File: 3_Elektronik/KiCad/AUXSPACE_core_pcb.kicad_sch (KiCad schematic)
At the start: 4 parts

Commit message: BOM:              added missing datasheets, added missing partnumbers, corrected partnumbers circit diagram:   adjusted values unified writing
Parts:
- R1, R3, R5, R7: WE_PTNBR (none) -> 560112116001
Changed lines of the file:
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@@
 			)
 		)
-		(property "Datasheet" ""
+		(property "Datasheet" "https://www.we-online.com/components/products/datasheet/560112116001.pdf"
 			(at 245.11 125.73 0)
 			(hide yes)
@@
 		(property "Description" "Resistor"
 			(at 245.11 125.73 0)
+			(hide yes)
+			(show_name no)
+			(do_not_autoplace no)
+			(effects
+				(font
+					(size 1.27 1.27)
+				)
+			)
+		)
+		(property "LCSC_PTNBR" ""
+			(at 245.11 125.73 90)
+			(hide yes)
+			(show_name no)
+			(do_not_autoplace no)
+			(effects
+				(font
+					(size 1.27 1.27)
+				)
+			)
+		)
+		(property "WE_PTNBR" "560112116001"
+			(at 245.11 125.73 90)
+			(hide yes)
+			(show_name no)
+			(do_not_autoplace no)
+			(effects
+				(font
+					(size 1.27 1.27)
+				)
+			)
+		)
+		(property "VOELKNER_PTNBR" ""
+			(at 245.11 125.73 90)
+			(hide yes)
+			(show_name no)
+			(do_not_autoplace no)
+			(effects
+				(font
+					(size 1.27 1.27)
+				)
+			)
+		)
+		(property "MOUSER_PTNBR" ""
+			(at 245.11 125.73 90)
 			(hide yes)
 			(show_name no)
@@
 			)
 		)
-		(property "Datasheet" ""
+		(property "Datasheet" "https://www.we-online.com/components/products/datasheet/560112116001.pdf"
 			(at 245.11 132.08 0)
 			(hide yes)
@@
 		(property "Description" "Resistor"
 			(at 245.11 132.08 0)
+			(hide yes)
+			(show_name no)
+			(do_not_autoplace no)
+			(effects
+				(font
+					(size 1.27 1.27)
+				)
+			)
+		)
+		(property "LCSC_PTNBR" ""
+			(at 245.11 132.08 90)
+			(hide yes)
+			(show_name no)
+			(do_not_autoplace no)
+			(effects
+				(font
+					(size 1.27 1.27)
+				)
+			)
+		)
+		(property "WE_PTNBR" "560112116001"
+			(at 245.11 132.08 90)
+			(hide yes)
+			(show_name no)
+			(do_not_autoplace no)
+			(effects
+				(font
+					(size 1.27 1.27)
+				)
+			)
+		)
+		(property "VOELKNER_PTNBR" ""
+			(at 245.11 132.08 90)
+			(hide yes)
+			(show_name no)
+			(do_not_autoplace no)
+			(effects
+				(font
+					(size 1.27 1.27)
+				)
+			)
+		)
+		(property "MOUSER_PTNBR" ""
+			(at 245.11 132.08 90)
 			(hide yes)
 			(show_name no)
@@
 			)
 		)
-		(property "Datasheet" ""
+		(property "Datasheet" "https://www.we-online.com/components/products/datasheet/560112116001.pdf"
 			(at 245.11 119.38 0)
 			(hide yes)
@@
 		(property "Description" "Resistor"
 			(at 245.11 119.38 0)
+			(hide yes)
+			(show_name no)
+			(do_not_autoplace no)
+			(effects
+				(font
+					(size 1.27 1.27)
+				)
+			)
+		)
+		(property "LCSC_PTNBR" ""
+			(at 245.11 119.38 90)
+			(hide yes)
+			(show_name no)
+			(do_not_autoplace no)
+			(effects
+				(font
+					(size 1.27 1.27)
+				)
+			)
+		)
+		(property "WE_PTNBR" "560112116001"
+			(at 245.11 119.38 90)
+			(hide yes)
+			(show_name no)
+			(do_not_autoplace no)
+			(effects
+				(font
+					(size 1.27 1.27)
+				)
+			)
+		)
+		(property "VOELKNER_PTNBR" ""
+			(at 245.11 119.38 90)
+			(hide yes)
+			(show_name no)
+			(do_not_autoplace no)
+			(effects
+				(font
+					(size 1.27 1.27)
+				)
+			)
+		)
+		(property "MOUSER_PTNBR" ""
+			(at 245.11 119.38 90)
 			(hide yes)
 			(show_name no)
@@
 			)
 		)
-		(property "Datasheet" ""
+		(property "Datasheet" "https://www.we-online.com/components/products/datasheet/560112116001.pdf"
 			(at 245.11 113.03 0)
 			(hide yes)
@@
 			(hide yes)
 			(show_name no)
+			(do_not_autoplace no)
+			(effects
+				(font
+					(size 1.27 1.27)
+				)
+			)
+		)
+		(property "LCSC_PTNBR" ""
+			(at 245.11 113.03 90)
+			(hide yes)
+			(show_name no)
+			(do_not_autoplace no)
+			(effects
+				(font
+					(size 1.27 1.27)
+				)
+			)
+		)
+		(property "WE_PTNBR" "560112116001"
+			(at 245.11 113.03 90)
+			(hide yes)
+			(show_name no)
+			(do_not_autoplace no)
+			(effects
+				(font
+					(size 1.27 1.27)
+				)
+			)
+		)
+		(property "VOELKNER_PTNBR" ""
+			(at 245.11 113.03 90)
+			(hide yes)
+			(show_name no)
+			(do_not_autoplace no)
+			(effects
+				(font
+					(size 1.27 1.27)
+				)
+			)
+		)
+		(property "MOUSER_PTNBR" ""
+			(at 245.11 113.03 90)
+			(hide yes)
+			(show_name no)

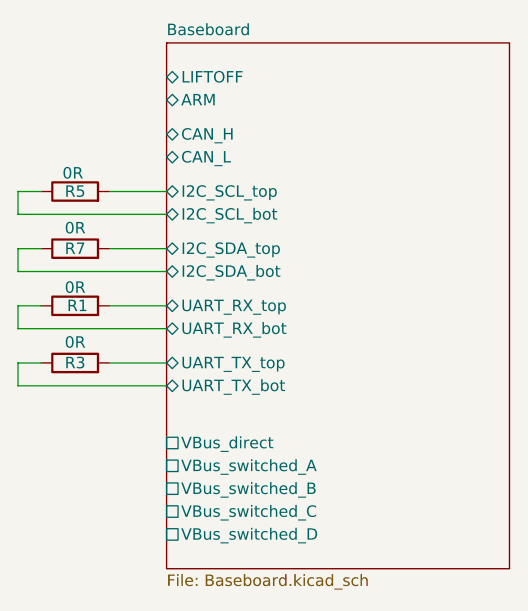
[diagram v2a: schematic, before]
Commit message: ci(drc): :green_heart: fix errors
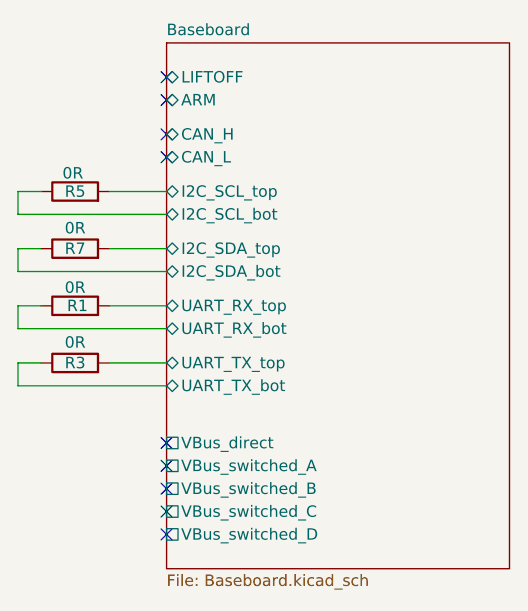
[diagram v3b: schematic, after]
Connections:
- no-connect marks 0 -> 9
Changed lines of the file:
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@@
 		)
+	)
+	(no_connect
+		(at 255.27 102.87)
+	)
+	(no_connect
+		(at 255.27 106.68)
+	)
+	(no_connect
+		(at 255.27 109.22)
+	)
+	(no_connect
+		(at 255.27 100.33)
+	)
+	(no_connect
+		(at 255.27 140.97)
+	)
+	(no_connect
+		(at 255.27 143.51)
+	)
+	(no_connect
+		(at 255.27 146.05)
+	)
+	(no_connect
+		(at 255.27 148.59)
+	)
+	(no_connect
+		(at 255.27 151.13)
 	)
 	(sheet_instances

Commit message: style: :art: split schematics into subpages
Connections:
- no-connect marks 9 -> 5
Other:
- added sheet MCU (mcu.kicad_sch)
- added sheet Power (power.kicad_sch)
- added sheet Sensors and Peripherals (sensors.kicad_sch)
- sheet Baseboard ports: added Bat_on_ext, Power_Fault; removed none
- moved on the sheet: R1, R3, R5, R7

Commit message: build: :wrench: swap baro with meas ms5607
Use the MS5607 since it can measure up to ~30km above sea level.
The DPS was only able to measure up to ~9km.
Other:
- sheet MCU ports: added none; removed BARO_INT
- sheet Sensors and Peripherals ports: added none; removed BARO_INT
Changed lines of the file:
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@@
+	(wire
+		(pts
+			(xy 182.88 111.76) (xy 191.77 111.76)
+		)
+		(stroke
+			(width 0)
+			(type default)
+		)
+	)
+	(wire
+		(pts
+			(xy 233.68 102.87) (xy 256.54 102.87)
+		)
+		(stroke
+			(width 0)
+			(type default)
+		)
+	)
+	(wire
+		(pts
+			(xy 240.03 116.84) (xy 242.57 116.84)
+		)
+		(stroke
+			(width 0)
+			(type default)
+		)
+	)
 	(wire
 		(pts
 			(xy 182.88 138.43) (xy 191.77 138.43)
-		)
-		(stroke
-			(width 0)
-			(type default)
-		)
-	)
-	(wire
-		(pts
-			(xy 182.88 111.76) (xy 191.77 111.76)
-		)
-		(stroke
-			(width 0)
-			(type default)
-		)
-	)
-	(wire
-		(pts
-			(xy 233.68 102.87) (xy 256.54 102.87)
-		)
-		(stroke
-			(width 0)
-			(type default)
-		)
-	)
-	(wire
-		(pts
-			(xy 240.03 116.84) (xy 242.57 116.84)
-		)
-		(stroke
-			(width 0)
-			(type default)
-		)
-	)
-	(wire
-		(pts
-			(xy 182.88 140.97) (xy 191.77 140.97)
 		)
 		(stroke
@@
 			)
 		)
-		(pin "BARO_INT" passive
+		(pin "Buzzer" passive
 			(at 191.77 138.43 180)
-			(effects
-				(font
-					(size 1.27 1.27)
-				)
-				(justify left)
-			)
-		)
-		(pin "Buzzer" passive
-			(at 191.77 140.97 180)
 			(effects
 				(font
@@
 			)
 		)
-		(pin "BARO_INT" passive
-			(at 182.88 138.43 0)
-			(effects
-				(font
-					(size 1.27 1.27)
-				)
-				(justify right)
-			)
-		)
 		(pin "I2C0_SCL" passive
 			(at 182.88 100.33 0)
@@
 		)
 		(pin "Buzzer" passive
-			(at 182.88 140.97 0)
-			(effects
-				(font
+			(at 182.88 138.43 0)
+			(effects
+				(font
